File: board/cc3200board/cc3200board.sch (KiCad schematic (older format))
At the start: 38 parts, among them U2 N25Q128A13ESE40E, X1 32.768kH, X2 ABM3B-40.000MHZ-10-1-U-T

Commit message: Committing final changes
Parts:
- C1, C10, C11, C12, C13, C14, C15, C16, C17, C18, C19, C2, C20, C22, C23, C3, C4, C5, C8, C9, L1, L2, L3, L8, R1, R2, R3, R4, U2, X1: footprint ~ -> (none)
- C24, C46: footprint ~ -> Capacitors_SMD:c_0805
- C42, C49: value 10.2pF -> 10pF; footprint ~ -> Capacitors_SMD:c_0805
- gave numbers to parts that had none: 1

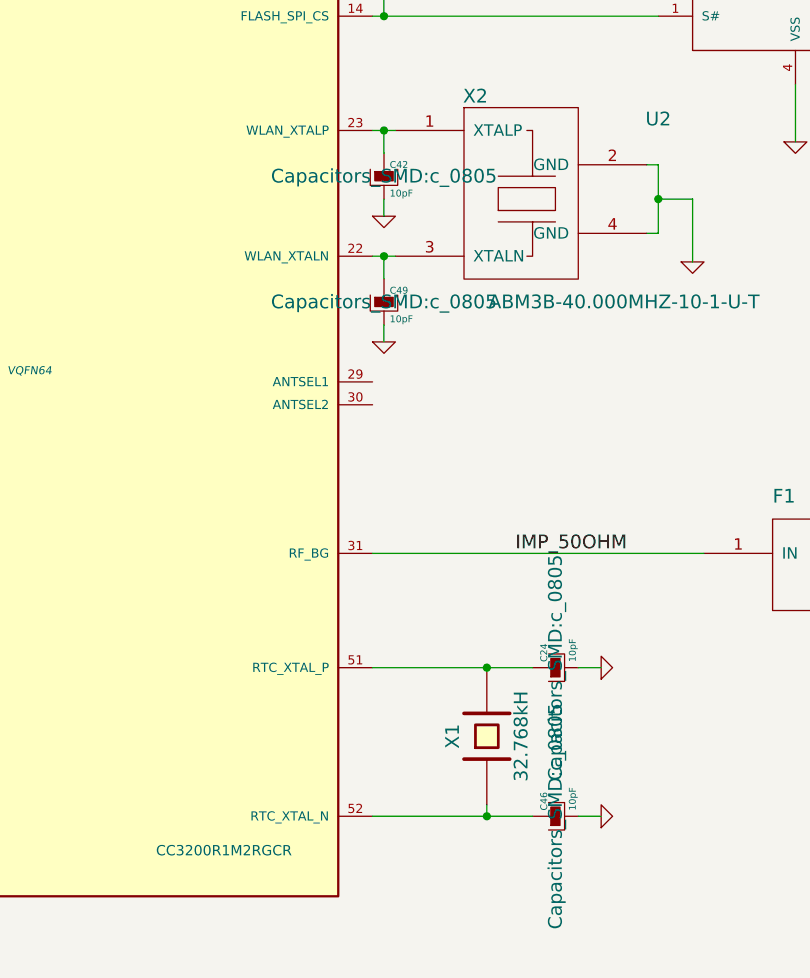
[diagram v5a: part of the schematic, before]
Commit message: Updated board-to-board interface definition with CC3200 GPIO lines
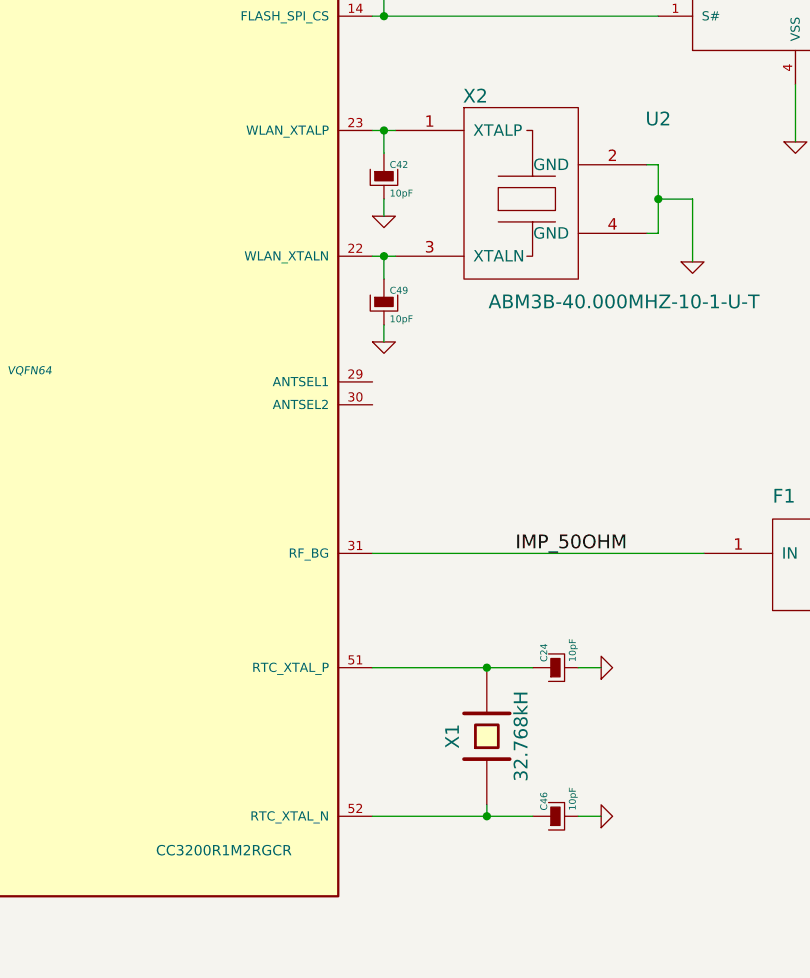
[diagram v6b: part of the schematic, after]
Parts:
- C24, C42, C46, C49: footprint Capacitors_SMD:c_0805 -> (none)
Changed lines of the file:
@@
 F 0 "C24" H 6525 6200 30  0000 L CNN
 F 1 "10pF" H 6525 6075 30  0000 L CNN
-F 2 "Capacitors_SMD:c_0805" H 6500 6150 60  0000 C CNN
+F 2 "" H 6500 6150 60  0000 C CNN
 F 3 "~" H 6500 6150 60  0000 C CNN
 	1    6500 6150
@@
 F 0 "C46" H 6525 6850 30  0000 L CNN
 F 1 "10pF" H 6525 6725 30  0000 L CNN
-F 2 "Capacitors_SMD:c_0805" H 6500 6800 60  0000 C CNN
+F 2 "" H 6500 6800 60  0000 C CNN
 F 3 "~" H 6500 6800 60  0000 C CNN
 	1    6500 6800
@@
 F 0 "C49" H 5775 4600 30  0000 L CNN
 F 1 "10pF" H 5775 4475 30  0000 L CNN
-F 2 "Capacitors_SMD:c_0805" H 5750 4550 60  0000 C CNN
+F 2 "" H 5750 4550 60  0000 C CNN
 F 3 "~" H 5750 4550 60  0000 C CNN
 	1    5750 4550
@@
 F 0 "C42" H 5775 4050 30  0000 L CNN
 F 1 "10pF" H 5775 3925 30  0000 L CNN
-F 2 "Capacitors_SMD:c_0805" H 5750 4000 60  0000 C CNN
+F 2 "" H 5750 4000 60  0000 C CNN
 F 3 "~" H 5750 4000 60  0000 C CNN
 	1    5750 4000

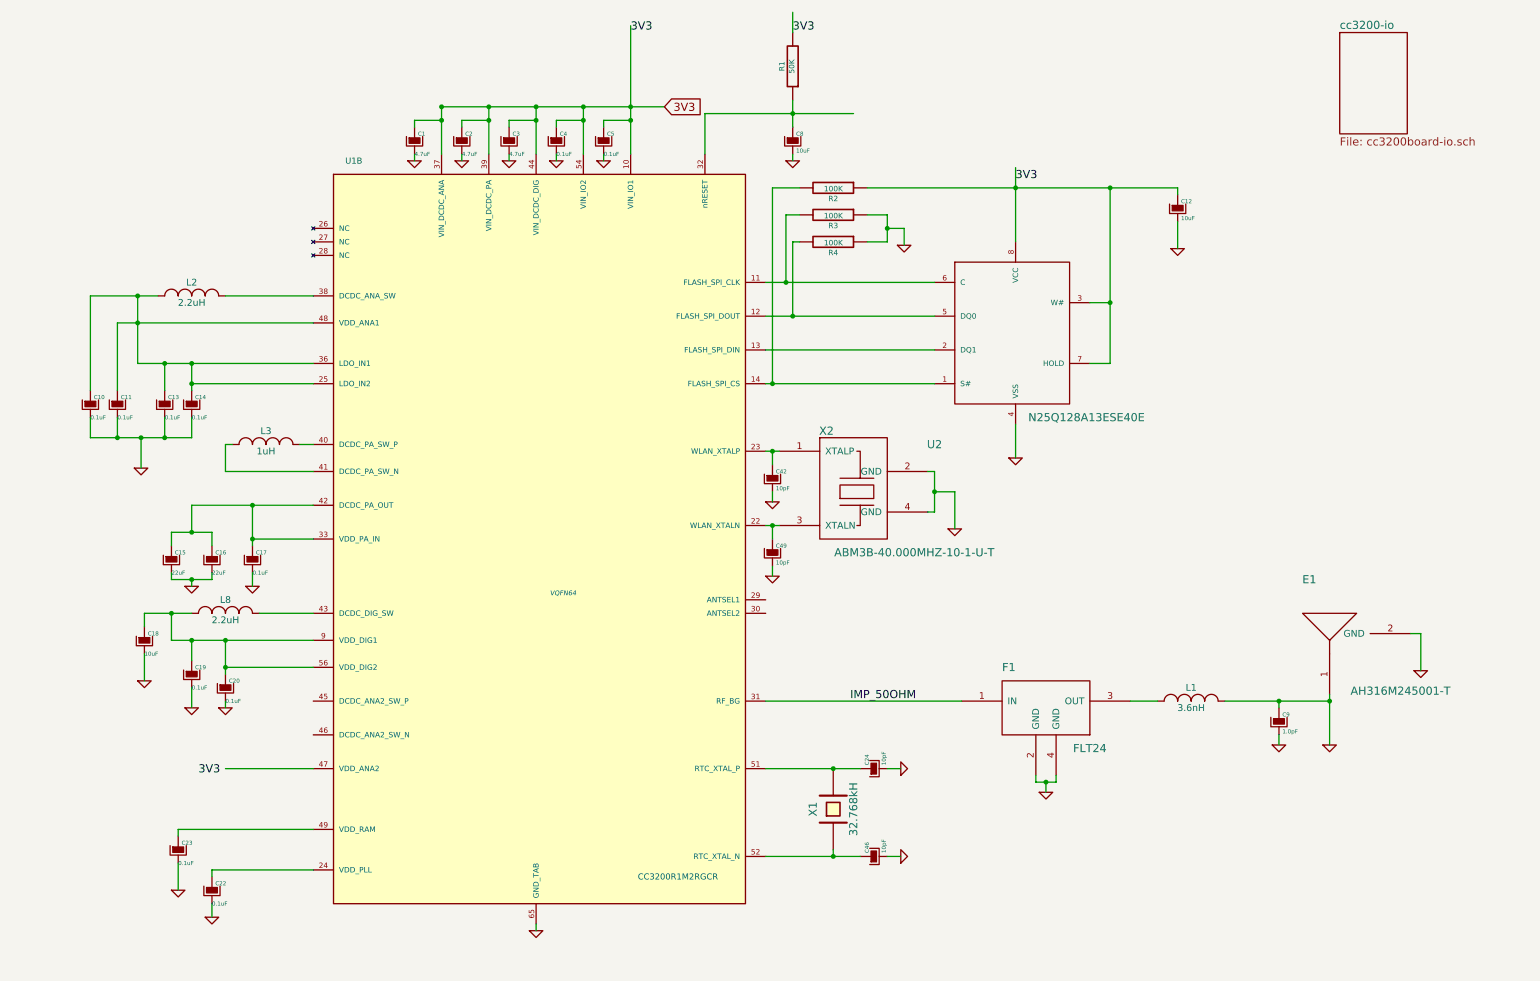
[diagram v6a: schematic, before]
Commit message: Finished schematic layout
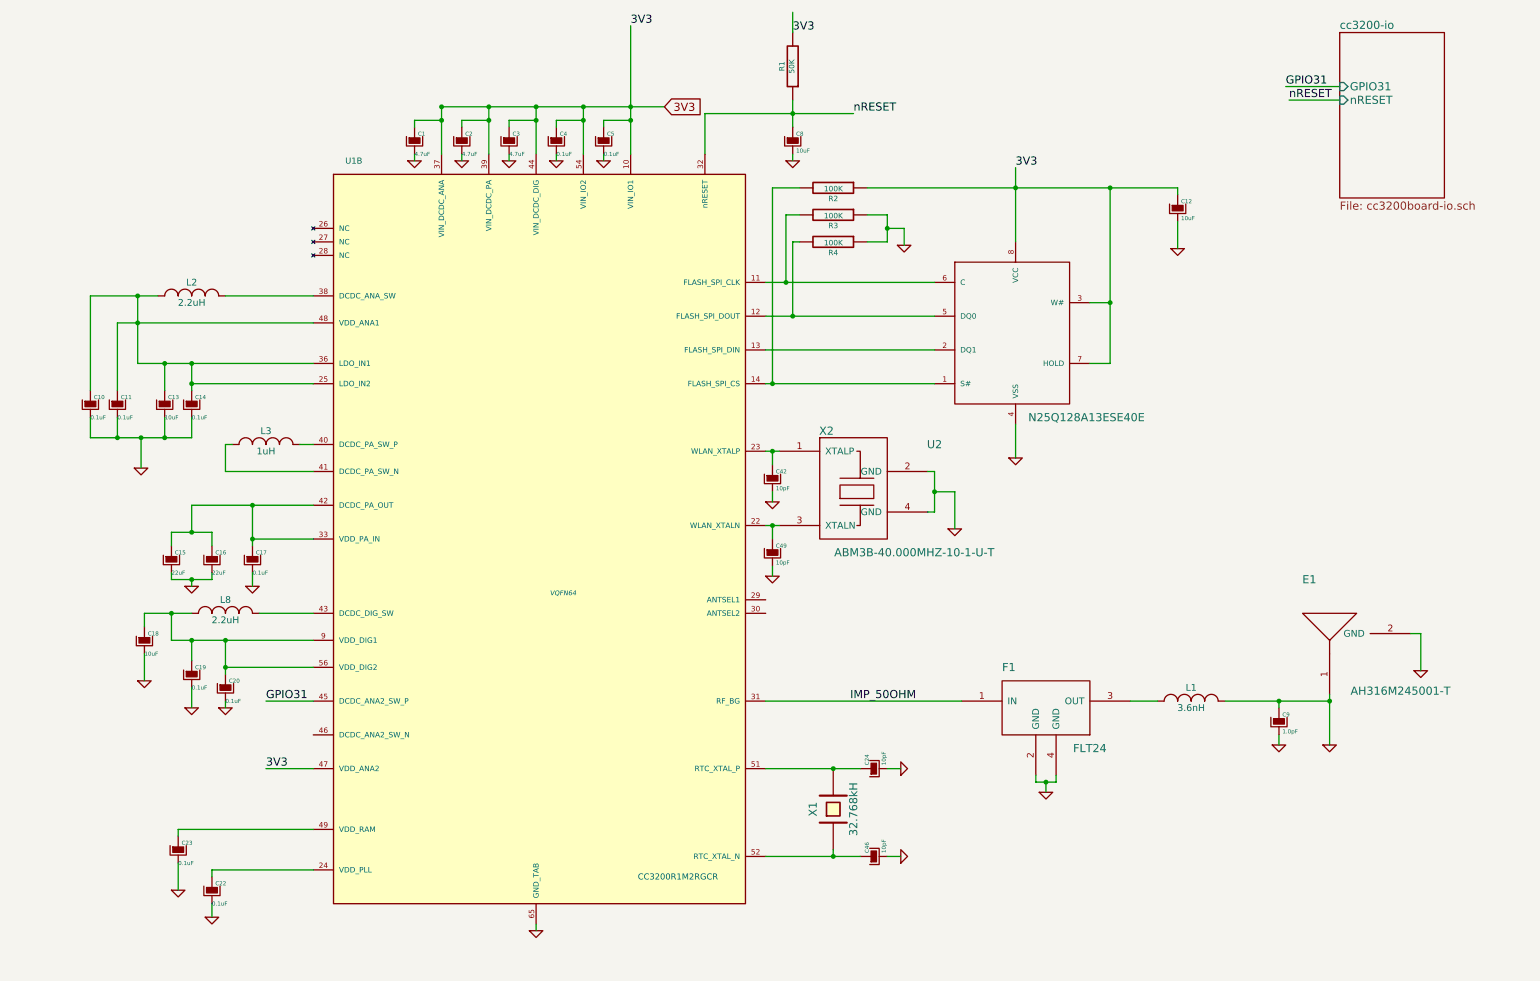
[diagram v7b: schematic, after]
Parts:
- C13: value 0.1uF -> 10uF
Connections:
- net labels added: GPIO31, nRESET
- wire segments 128 -> 131
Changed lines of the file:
@@
 P 1250 3450
 F 0 "C13" H 1275 3500 30  0000 L CNN
-F 1 "0.1uF" H 1250 3350 30  0000 L CNN
+F 1 "10uF" H 1250 3350 30  0000 L CNN
 F 2 "" H 1250 3450 60  0000 C CNN
 F 3 "~" H 1250 3450 60  0000 C CNN
@@
 Text Label 5900 700  0    60   ~ 0
 3V3
-Text Label 4700 700  0    60   ~ 0
+Text Label 4700 650  0    60   ~ 0
 3V3
 $Comp
@@
 	0    -1   -1   0
 $EndComp
-Text Label 1500 6200 0    60   ~ 0
+Text Label 2000 6150 0    60   ~ 0
 3V3
 $Comp
@@
 	1    0    0    -1
 $EndComp
-Text Label 7550 1800 0    60   ~ 0
+Text Label 7550 1700 0    60   ~ 0
 3V3
 $Comp
@@
 Connection ~ 1450 5200
 Wire Wire Line
-	2350 6150 1700 6150
+	2350 6150 2000 6150
 Wire Wire Line
 	1300 4500 1300 4400
@@
 	8100 2700 8250 2700
 Connection ~ 8250 2700
+Text Label 6325 5650 0    60   ~ 0
+IMP_50OHM
+Wire Wire Line
+	2000 5650 2350 5650
+Text Label 2000 5650 0    60   ~ 0
+GPIO31
+Wire Wire Line
+	9950 1100 9550 1100
+Text Label 9550 1100 0    60   ~ 0
+GPIO31
 $Sheet
-S 9950 700  500  750
+S 9950 700  775  1225
 U 5452FF59
 F0 "cc3200-io" 60
 F1 "cc3200board-io.sch" 60
+F2 "GPIO31" I L 9950 1100 60
+F3 "nRESET" I L 9950 1200 60
 $EndSheet
-Text Label 6325 5650 0    60   ~ 0
-IMP_50OHM
+Wire Wire Line
+	9950 1200 9575 1200
+Text Label 6350 1300 0    60   ~ 0
+nRESET
+Text Label 9575 1200 0    60   ~ 0
+nRESET
 $EndSCHEMATC

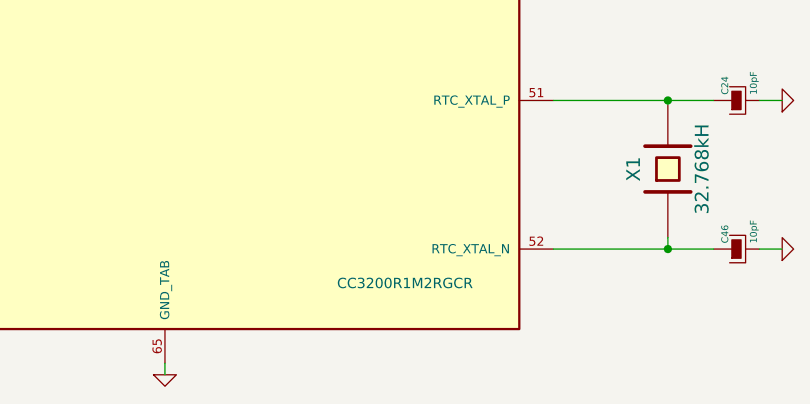
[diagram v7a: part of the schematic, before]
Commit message: Fixed mirrored footprint, outlines
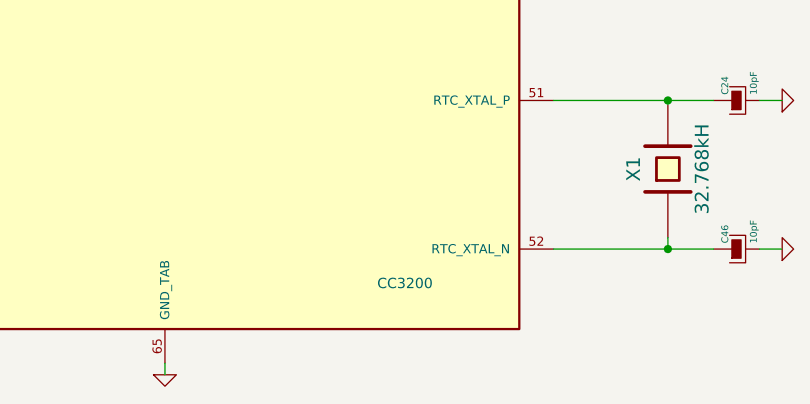
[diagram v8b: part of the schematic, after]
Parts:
- U1: value CC3200R1M2RGCR -> CC3200
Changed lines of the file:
@@
 LIBS:valves
 LIBS:cc3200board
+LIBS:mainboard
 LIBS:cc3200board-cache
 EELAYER 25 0
@@
 P 4000 4450
 F 0 "U1" H 2650 7250 45  0000 C CNN
-F 1 "CC3200R1M2RGCR" H 5050 1950 45  0000 C CNN
+F 1 "CC3200" H 5050 1950 45  0000 C CNN
 F 2 "VQFN64" H 4200 4050 35  0000 C CIN
 F 3 "~" H 4350 4200 60  0000 C CNN
